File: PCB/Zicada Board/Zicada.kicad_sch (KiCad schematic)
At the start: 55 parts, among them J1 Conn_ARM_JTAG_SWD_10, J2 Conn_01x01_Pin, J3 Conn_01x01_Pin, SW1 SW_Push, U1 nRF52840, U2 HDC2080, U3 SM351LT, U4 TPS610981, Y1 32MHz, Y2 32.768kHz

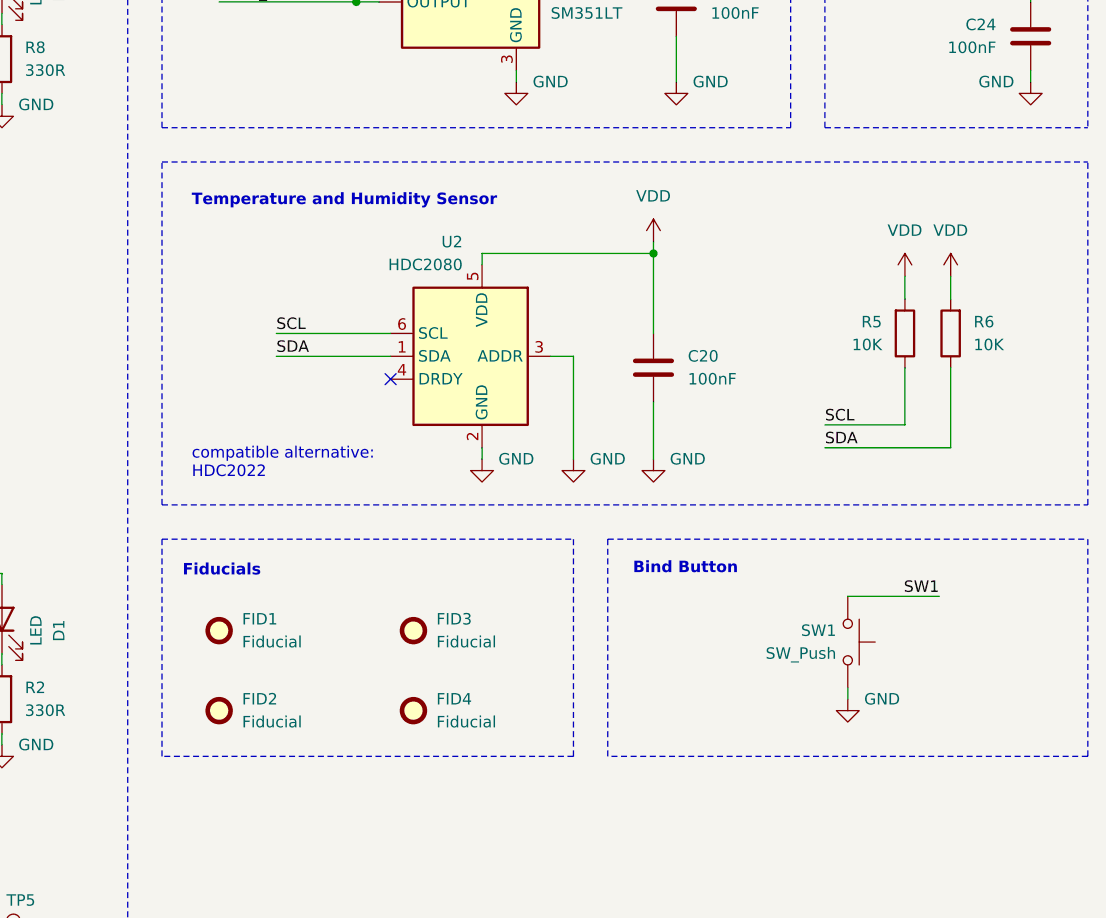
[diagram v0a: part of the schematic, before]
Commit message: Added OPT3001 sensor
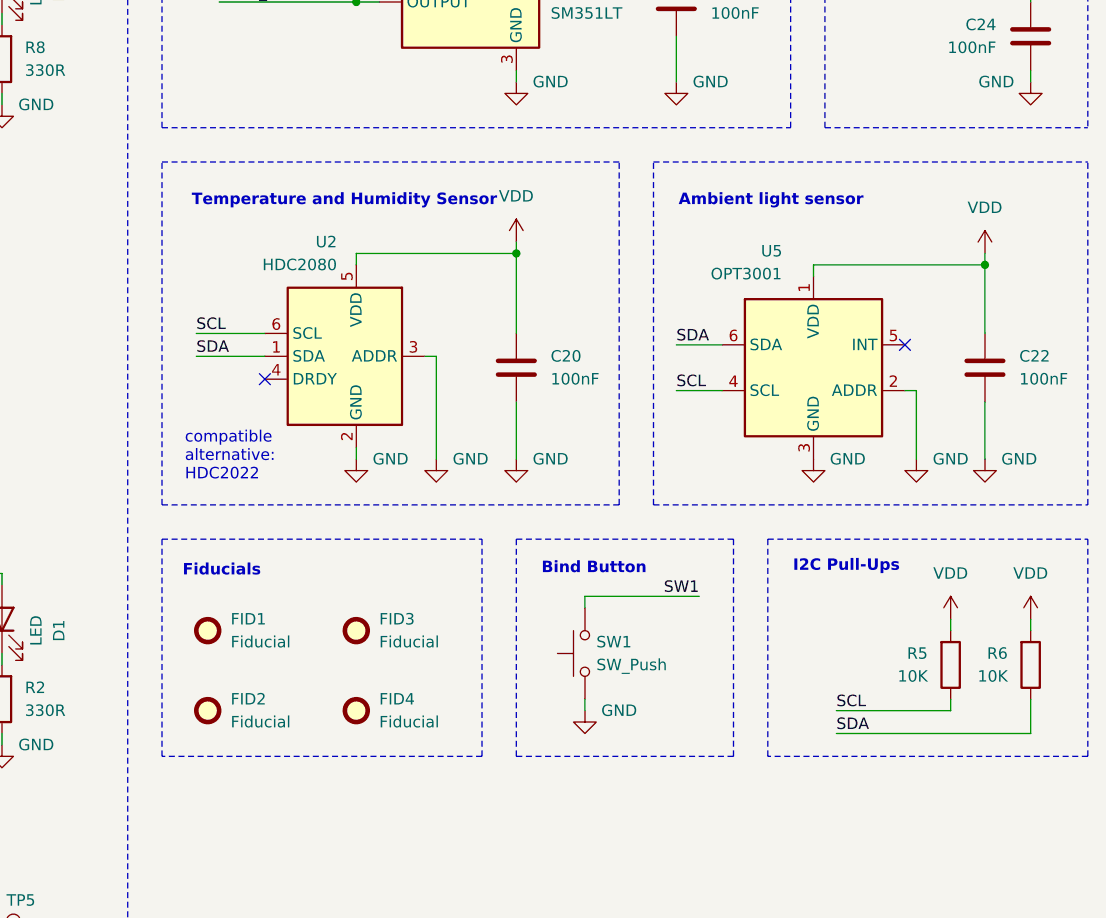
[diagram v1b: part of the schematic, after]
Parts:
- added C22: 100nF, Capacitor_SMD:C_0603_1608Metric, symbol Device:C
- added U5: OPT3001, zicadaLib:USON-6-1EP_2x2mm_P0.65mm_EP0.65x1.35mm, symbol zicadaLib:OPT3001
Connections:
- net GND: now also C22.2, U5.2 (ADDR), U5.3 (GND)
- net SCL: now also U5.4 (SCL)
- net SDA: now also U5.6 (SDA)
- net VDD: now also C22.1, U5.1 (VDD)
- no-connect marks 8 -> 9
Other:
- note added: "Ambient light sensor"
- note added: "I2C Pull-Ups"
- moved on the sheet: C20, FID1, FID2, FID3, FID4, R5, R6, SW1, U2

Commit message: generated fabrication files
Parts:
- F1: LCSC C3761461 -> C207021
- U5: LCSC (none) -> C90462
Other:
- note added: "Ambient Light Sensor"
- note removed: "Ambient light sensor"
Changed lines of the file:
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@@
 			(font
 				(size 1.27 1.27)
+				(thickness 0.254)
+				(bold yes)
 			)
 		)
 	)
-	(text "Ambient light sensor"
+	(text "Ambient Light Sensor"
 		(exclude_from_sim no)
 		(at 236.474 101.6 0)
@@
 			)
 		)
+		(property "LCSC" "C90462"
+			(at 251.46 119.38 0)
+			(effects
+				(font
+					(size 1.27 1.27)
+				)
+				(hide yes)
+			)
+		)
 		(pin "2"
 		)
@@
 			)
 		)
-		(property "LCSC" "C3761461"
+		(property "LCSC" "C207021"
 			(at 205.74 34.29 90)
 			(effects
